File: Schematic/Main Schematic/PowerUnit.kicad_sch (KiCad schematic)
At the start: 20 parts, among them J6 USB_B_Micro

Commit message: Update
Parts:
- BT?: footprint Battery:BatteryHolder_Keystone_3034_1x20mm -> A_New_folder:18650_Holder_SMD
- C?: footprint Capacitor_SMD:C_1206_3216Metric_Pad1.33x1.80mm_HandSolder -> A_New_folder:C1206
- IC?: footprint SOT95P280X135-6N -> (none)
- J6: footprint (none) -> A_New_folder:USB_Conn_JLC_LCSC_C404969
- Q?: footprint SOP65P640X120-8N -> (none)
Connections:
- net D12: now reaches Q?.1 (D12_1)
- net D12: now also Q?.8 (D12_2)
- no-connect marks 3 -> 1
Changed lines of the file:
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@@
   (junction (at 142.24 45.72) (diameter 0) (color 0 0 0 0)
   )
-  (no_connect (at 152.4 78.74))
-  (no_connect (at 182.88 78.74))
   (no_connect (at 177.8 60.96))
   (wire (pts (xy 85.852 162.6108) (xy 85.852 167.6908))
@@
     (effects (font (size 1.27 1.27)) (justify left bottom))
   )
+  (label "D12" (at 182.88 78.74 0) (fields_autoplaced)
+    (effects (font (size 1.27 1.27)) (justify left bottom))
+  )
   (label "V1" (at 260.35 58.42 0) (fields_autoplaced)
     (effects (font (size 1.27 1.27)) (justify left bottom))
@@
   (label "5V" (at 39.4208 68.58 0) (fields_autoplaced)
     (effects (font (size 1.27 1.27)) (justify left bottom))
+  )
+  (label "D12" (at 152.4 78.74 180) (fields_autoplaced)
+    (effects (font (size 1.27 1.27)) (justify right bottom))
   )
   (global_label "USB D+" (shape input) (at 44.5008 73.66 0) (fields_autoplaced)
@@
       (effects (font (size 1.27 1.27)))
     )
-    (property "Footprint" "SOP65P640X120-8N" (at 179.07 173.66 0)
+    (property "Footprint" "" (at 179.07 173.66 0)
       (effects (font (size 1.27 1.27)) (justify left top) hide)
     )
@@
       (effects (font (size 1.27 1.27)))
     )
-    (property "Footprint" "" (at 34.036 74.93 0)
+    (property "Footprint" "A_New_folder:USB_Conn_JLC_LCSC_C404969" (at 34.036 74.93 0)
       (effects (font (size 1.27 1.27)) hide)
     )
@@
       (effects (font (size 1.27 1.27)))
     )
-    (property "Footprint" "SOT95P280X135-6N" (at 173.99 150.8 0)
+    (property "Footprint" "" (at 173.99 150.8 0)
       (effects (font (size 1.27 1.27)) (justify left top) hide)
     )
@@
       (effects (font (size 1.27 1.27)) (justify left))
     )
-    (property "Footprint" "Capacitor_SMD:C_1206_3216Metric_Pad1.33x1.80mm_HandSolder" (at 203.2 71.12 0)
+    (property "Footprint" "A_New_folder:C1206" (at 203.2 71.12 0)
       (effects (font (size 1.27 1.27)) hide)
     )
@@
       (effects (font (size 1.27 1.27)) (justify left))
     )
-    (property "Footprint" "Battery:BatteryHolder_Keystone_3034_1x20mm" (at 251.46 72.136 90)
-      (effects (font (size 1.27 1.27)) hide)
-    )
+    (property "Footprint" "A_New_folder:18650_Holder_SMD" (at 251.46 72.136 90)
+      (effects (font (size 1.27 1.27)) hide)
+    )

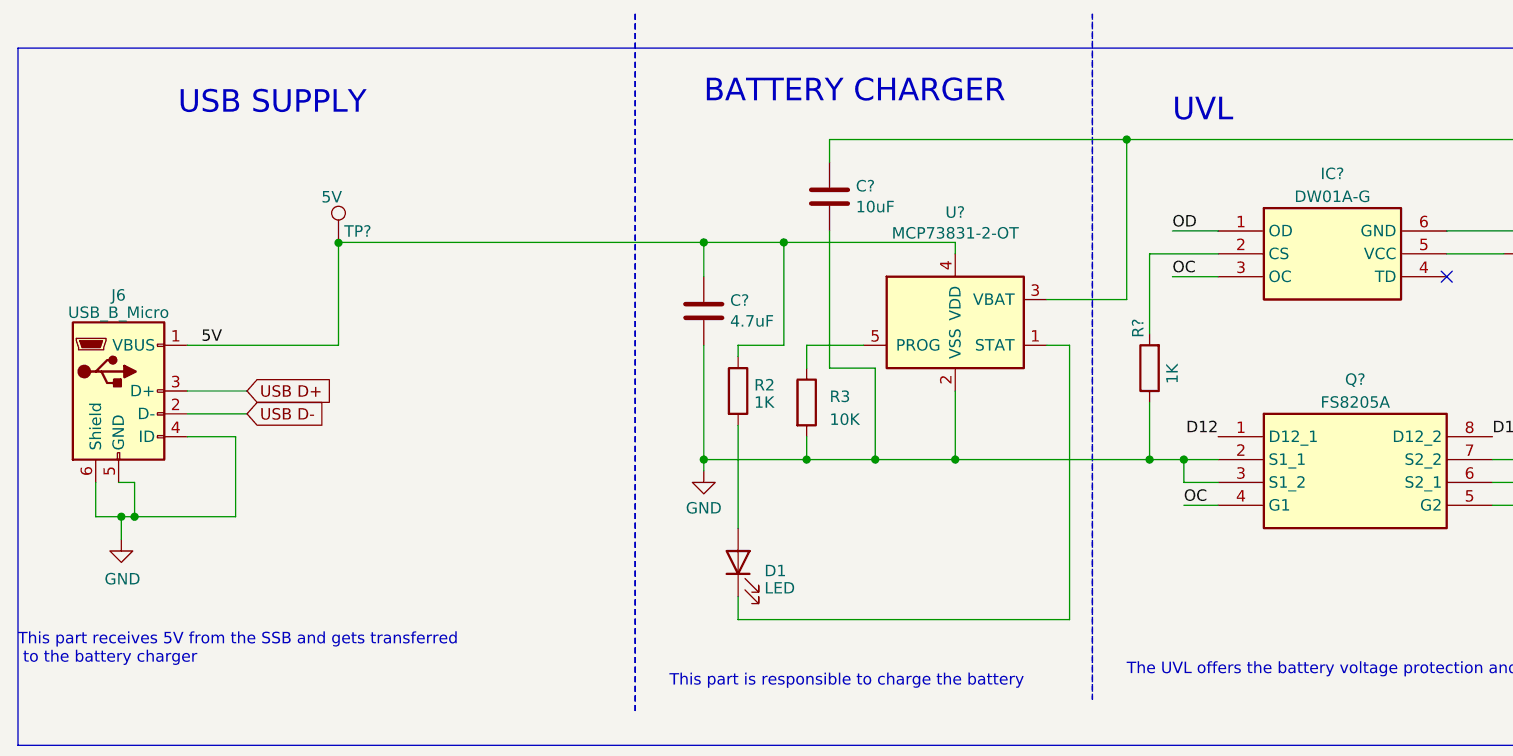
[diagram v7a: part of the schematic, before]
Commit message: Footprints all added and the PCB has been created but not placed according to the proper configuration
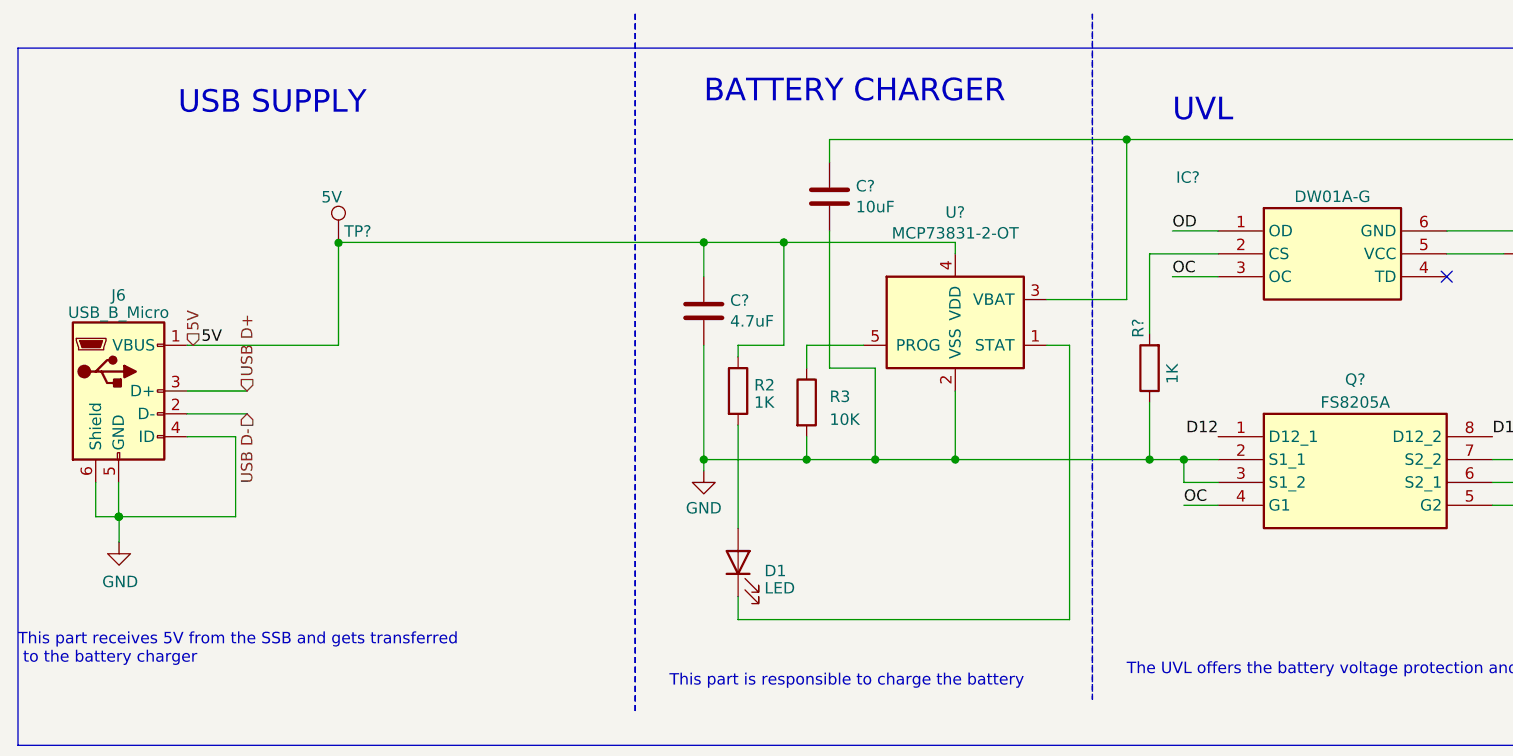
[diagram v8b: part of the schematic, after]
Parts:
- D1: footprint Capacitor_SMD:C_1206_3216Metric -> LED_THT:LED_D3.0mm
- IC?: footprint (none) -> A_New_folder:SOT-23-6_L2.9-W1.6-P0.95-LS2.8-BR
- J6: footprint A_New_folder:USB_Conn_JLC_LCSC_C404969 -> A_New_folder:MICRO-USB-SMD_MICROXNJ
- Q?: footprint (none) -> A_New_folder:TSSOP-8_L4.4-W3.0-P0.65-LS6.4-BL-2
- R2, R?: footprint 1K_R:RESC1005X40N -> A_New_folder:R0402
- R?: footprint 100_R:RESC1608X55N -> A_New_folder:R0603
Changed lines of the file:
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@@
   (junction (at 144.78 81.28) (diameter 0) (color 0 0 0 0)
   )
-  (junction (at 30.5308 87.63) (diameter 0) (color 0 0 0 0)
+  (junction (at 30.2768 87.63) (diameter 0) (color 0 0 0 0)
   )
   (junction (at 95.25 81.28) (diameter 0) (color 0 0 0 0)
@@
   (junction (at 251.46 83.82) (diameter 0) (color 0 0 0 0)
   )
+  (junction (at 30.226 87.63) (diameter 0) (color 0 0 0 0)
+  )
   (junction (at 95.25 57.15) (diameter 0) (color 0 0 0 0)
   )
@@
   )
   (junction (at 195.58 83.82) (diameter 0) (color 0 0 0 0)
-  )
-  (junction (at 32.004 87.63) (diameter 0) (color 0 0 0 0)
   )
   (junction (at 104.14 57.15) (diameter 0) (color 0 0 0 0)
@@
     (stroke (width 0) (type default))
   )
-  (wire (pts (xy 32.004 87.63) (xy 43.2308 87.63))
+  (wire (pts (xy 27.686 87.63) (xy 30.226 87.63))
     (stroke (width 0) (type default))
   )
@@
     (stroke (width 0) (type default))
   )
+  (wire (pts (xy 30.2768 87.63) (xy 43.2308 87.63))
+    (stroke (width 0) (type default))
+  )
   (wire (pts (xy 177.8 55.88) (xy 195.58 55.88))
     (stroke (width 0) (type default))
@@
     (stroke (width 0) (type default))
   )
+  (wire (pts (xy 30.226 87.63) (xy 30.2768 87.63))
+    (stroke (width 0) (type default))
+  )
   (wire (pts (xy 135.89 68.58) (xy 135.89 99.06))
     (stroke (width 0) (type default))
@@
     (stroke (width 0) (type default))
   )
-  (wire (pts (xy 27.686 87.63) (xy 30.5308 87.63))
-    (stroke (width 0) (type default))
-  )
   (wire (pts (xy 123.19 58.42) (xy 123.19 57.15))
     (stroke (width 0) (type default))
@@
     (stroke (width 0) (type default))
   )
+  (wire (pts (xy 30.2768 90.4748) (xy 30.2768 87.63))
+    (stroke (width 0) (type default))
+  )
   (wire (pts (xy 53.086 148.59) (xy 56.4896 148.59))
     (stroke (width 0) (type default))
@@
     (stroke (width 0) (type default))
   )
-  (wire (pts (xy 32.004 83.82) (xy 32.004 87.63))
-    (stroke (width 0) (type default))
-  )
   (wire (pts (xy 109.22 45.72) (xy 109.22 48.26))
     (stroke (width 0) (type default))
@@
     (stroke (width 0) (type default))
   )
+  (wire (pts (xy 30.226 83.82) (xy 30.226 87.63))
+    (stroke (width 0) (type default))
+  )
   (wire (pts (xy 114.3 71.12) (xy 114.3 81.28))
     (stroke (width 0) (type default))
@@
     (stroke (width 0) (type default))
   )
-  (wire (pts (xy 30.5308 90.17) (xy 30.5308 87.63))
-    (stroke (width 0) (type default))
-  )
   (wire (pts (xy 142.24 45.72) (xy 203.2 45.72))
     (stroke (width 0) (type default))
@@
     (stroke (width 0) (type default))
   )
-  (wire (pts (xy 30.5308 87.63) (xy 32.004 87.63))
-    (stroke (width 0) (type default))
-  )
   (wire (pts (xy 203.2 77.47) (xy 203.2 83.82))
     (stroke (width 0) (type default))
@@
   )
   (wire (pts (xy 37.846 68.58) (xy 54.6608 68.58))
-    (stroke (width 0) (type default))
-  )
-  (wire (pts (xy 30.226 83.82) (xy 32.004 83.82))
     (stroke (width 0) (type default))
   )
@@
     (effects (font (size 1.27 1.27)) (justify right bottom))
   )
-  (global_label "USB D+" (shape input) (at 44.5008 73.66 0) (fields_autoplaced)
+  (hierarchical_label "USB D+" (shape input) (at 44.5008 73.66 90) (fields_autoplaced)
     (effects (font (size 1.27 1.27)) (justify left))
-    (property "Intersheetrefs" "${INTERSHEET_REFS}" (at 54.821 73.66 0)
-      (effects (font (size 1.27 1.27)) (justify left) hide)
-    )
-  )
-  (global_label "USB D-" (shape input) (at 44.5008 76.2 0) (fields_autoplaced)
+  )
+  (hierarchical_label "USB D-" (shape input) (at 44.5008 76.2 270) (fields_autoplaced)
+    (effects (font (size 1.27 1.27)) (justify right))
+  )
+  (hierarchical_label "5V" (shape input) (at 38.5064 68.58 90) (fields_autoplaced)
     (effects (font (size 1.27 1.27)) (justify left))
-    (property "Intersheetrefs" "${INTERSHEET_REFS}" (at 54.821 76.2 0)
-      (effects (font (size 1.27 1.27)) (justify left) hide)
-    )
   )
   (hierarchical_label "3.3V" (shape input) (at 102.87 148.59 0) (fields_autoplaced)
@@
       (effects (font (size 1.27 1.27)))
     )
-    (property "Footprint" "" (at 179.07 173.66 0)
+    (property "Footprint" "A_New_folder:TSSOP-8_L4.4-W3.0-P0.65-LS6.4-BL-2" (at 179.07 173.66 0)
       (effects (font (size 1.27 1.27)) (justify left top) hide)
     )
@@
       (effects (font (size 1.27 1.27)))
     )
-    (property "Footprint" "A_New_folder:USB_Conn_JLC_LCSC_C404969" (at 34.036 74.93 0)
+    (property "Footprint" "A_New_folder:MICRO-USB-SMD_MICROXNJ" (at 34.036 74.93 0)
       (effects (font (size 1.27 1.27)) hide)
     )
@@
       (effects (font (size 1.27 1.27)) (justify right))
     )
-    (property "Footprint" "Capacitor_SMD:C_1206_3216Metric" (at 99.06 92.71 0)
+    (property "Footprint" "LED_THT:LED_D3.0mm" (at 99.06 92.71 0)
       (effects (font (size 1.27 1.27)) hide)
     )
@@
       (effects (font (size 1.27 1.27)))
     )
-    (property "Footprint" "100_R:RESC1608X55N" (at 187.96 60.198 90)
+    (property "Footprint" "A_New_folder:R0603" (at 187.96 60.198 90)
       (effects (font (size 1.27 1.27)) hide)
     )
@@
       (effects (font (size 1.27 1.27)))
     )
-    (property "Footprint" "1K_R:RESC1005X40N" (at 146.558 71.12 90)
+    (property "Footprint" "A_New_folder:R0402" (at 146.558 71.12 90)
       (effects (font (size 1.27 1.27)) hide)
     )
@@
       (effects (font (size 1.27 1.27)) (justify left))
     )
-    (property "Footprint" "1K_R:RESC1005X40N" (at 97.282 73.66 90)
+    (property "Footprint" "A_New_folder:R0402" (at 97.282 73.66 90)
       (effects (font (size 1.27 1.27)) hide)
     )
@@
   )
   (symbol (lib_id "DW01A-G:DW01A-G") (at 152.4 55.88 0) (unit 1)
-    (in_bom yes) (on_board yes) (dnp no) (fields_autoplaced)
-    (property "Reference" "IC?" (at 165.1 49.53 0)
+    (in_bom yes) (on_board yes) (dnp no)
+    (property "Reference" "IC?" (at 149.0472 49.9364 0)
       (effects (font (size 1.27 1.27)))
     )
@@
       (effects (font (size 1.27 1.27)))
     )
-    (property "Footprint" "" (at 173.99 150.8 0)
+    (property "Footprint" "A_New_folder:SOT-23-6_L2.9-W1.6-P0.95-LS2.8-BR" (at 173.99 150.8 0)
       (effects (font (size 1.27 1.27)) (justify left top) hide)
     )
@@
     )
   )
-  (symbol (lib_id "power:GND") (at 30.5308 90.17 0) (unit 1)
+  (symbol (lib_id "power:GND") (at 30.2768 90.4748 0) (unit 1)
     (in_bom yes) (on_board yes) (dnp no)
-    (property "Reference" "#PWR?" (at 30.5308 96.52 0)
-      (effects (font (size 1.27 1.27)) hide)
-    )
-    (property "Value" "GND" (at 30.6578 94.5642 0)
-      (effects (font (size 1.27 1.27)))
-    )
-    (property "Footprint" "" (at 30.5308 90.17 0)
-      (effects (font (size 1.27 1.27)) hide)
-    )
-    (property "Datasheet" "" (at 30.5308 90.17 0)
-      (effects (font (size 1.27 1.27)) hide)
-    )
+    (property "Reference" "#PWR?" (at 30.2768 96.8248 0)
+      (effects (font (size 1.27 1.27)) hide)
+    )
+    (property "Value" "GND" (at 30.4038 94.869 0)
+      (effects (font (size 1.27 1.27)))
+    )
+    (property "Footprint" "" (at 30.2768 90.4748 0)
+      (effects (font (size 1.27 1.27)) hide)
+    )
+    (property "Datasheet" "" (at 30.2768 90.4748 0)
+      (effects (font (size 1.27 1.27)) hide)
+    )
